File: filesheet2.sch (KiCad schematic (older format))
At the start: 16 parts, among them J2 Conn Screen 1, J4 Conn Screen 2, SW25 Rotary_Encoder_Switch, SW26 SW_PUSH, U5 ATMEGA32U4, Y1 16Mhz

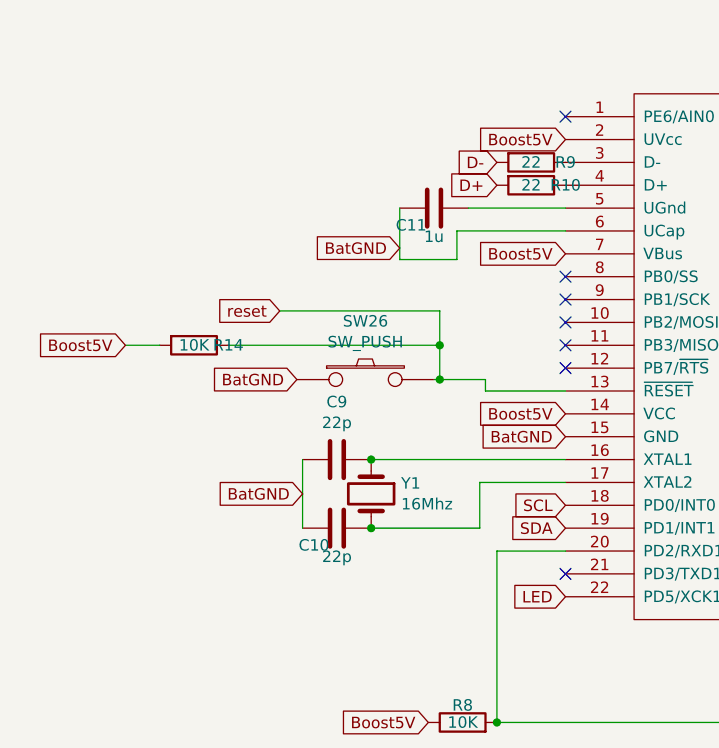
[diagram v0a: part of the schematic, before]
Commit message: Update kicad
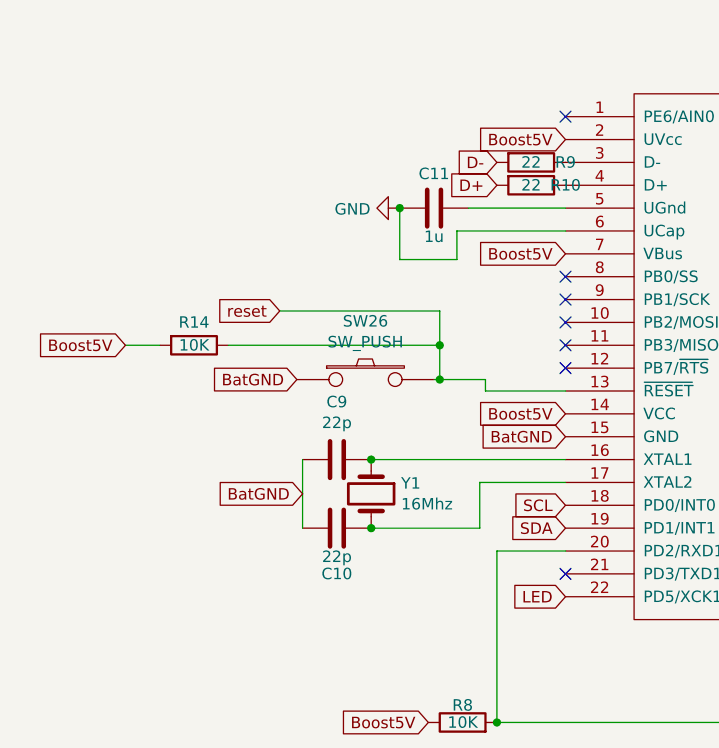
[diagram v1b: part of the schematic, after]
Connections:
- net BatGND: no longer C11.2, U5.6 (UCap)
- new net GND: C11.2, U5.6 (UCap)
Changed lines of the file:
@@
 U 1 1 5E794A2D
 P 2650 3750
-F 0 "C10" V 2725 3650 50  0000 C CNN
+F 0 "C10" V 2850 3750 50  0000 C CNN
 F 1 "22p" V 2775 3750 50  0000 C CNN
 F 2 "" H 2688 3600 50  0001 C CNN
@@
 U 1 1 5E797081
 P 3075 2350
-F 0 "C11" V 3150 2250 50  0000 C CNN
+F 0 "C11" V 2925 2350 50  0000 C CNN
 F 1 "1u" V 3200 2350 50  0000 C CNN
 F 2 "" H 3113 2200 50  0001 C CNN
@@
 Text GLabel 3350 2250 0    50   Input ~ 0
 D+
-Text GLabel 2925 2525 0    50   Input ~ 0
-BatGND
 Text GLabel 3650 2550 0    50   Input ~ 0
 Boost5V
@@
 U 1 1 5E808A49
 P 2025 2950
-F 0 "R14" V 2025 3100 50  0000 C CNN
+F 0 "R14" V 1925 2950 50  0000 C CNN
 F 1 "10K" V 2025 2950 50  0000 C CNN
 F 2 "" V 1955 2950 50  0001 C CNN
@@
 Text GLabel 7375 3775 2    50   Input ~ 0
 SCL
+$Comp
+L power:GND #PWR0101
+U 1 1 5EAEFF13
+P 2925 2350
+F 0 "#PWR0101" H 2925 2100 50  0001 C CNN
+F 1 "GND" V 2930 2222 50  0000 R CNN
+F 2 "" H 2925 2350 50  0001 C CNN
+F 3 "" H 2925 2350 50  0001 C CNN
+	1    2925 2350
+	0    1    1    0
+$EndComp
+Connection ~ 2925 2350
 $EndSCHEMATC

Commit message: Update
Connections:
- net Boost5V is gone; now on net +5V: J2.3 (Pin_3), J4.3 (Pin_3), R11.2, R12.1, R14.2, R8.1, U5.14 (VCC), U5.2 (UVcc), U5.34 (VCC), U5.44 (AVCC), U5.7 (VBus)
- net BatGND renamed +5V
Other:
- moved on the sheet: R13
